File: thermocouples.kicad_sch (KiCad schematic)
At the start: 52 parts, among them J300 Conn_01x02_Pin, J301 Conn_01x02_Pin, J302 Conn_01x02_Pin, J303 Conn_01x02_Pin, U300 MAX31856, U301 MAX31856, U302 MAX31856, U303 MAX31856

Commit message: Some changes to power circuitry, more layout
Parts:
- C300, C301, C302, C303, C304, C305, C306, C307, C308, C309, C310, C311, C312, C313, C314, C315, C316, C317, C318, C319: footprint Capacitor_SMD:C_01005_0402Metric -> Capacitor_SMD:C_0402_1005Metric
- D300, D301, D302, D303: footprint Capacitor_SMD:C_01005_0402Metric -> LED_SMD:LED_0402_1005Metric
- R300, R301, R302, R303, R304, R305, R310, R311, R312, R313, R314, R315: footprint Resistor_SMD:R_0201_0603Metric -> Resistor_SMD:R_0603_1608Metric
- R306, R307, R308, R309, R316, R317, R318, R319: footprint Resistor_SMD:R_01005_0402Metric -> Resistor_SMD:R_0402_1005Metric
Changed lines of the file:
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@@
 			)
 		)
-		(property "Footprint" "Resistor_SMD:R_0201_0603Metric"
+		(property "Footprint" "Resistor_SMD:R_0603_1608Metric"
 			(at 174.244 84.074 90)
 			(effects
@@
 			)
 		)
-		(property "Footprint" "Resistor_SMD:R_01005_0402Metric"
+		(property "Footprint" "Resistor_SMD:R_0402_1005Metric"
 			(at 244.856 108.204 90)
 			(effects
@@
 			)
 		)
-		(property "Footprint" "Capacitor_SMD:C_01005_0402Metric"
+		(property "Footprint" "Capacitor_SMD:C_0402_1005Metric"
 			(at 69.5452 116.84 0)
 			(effects
@@
 			)
 		)
-		(property "Footprint" "Resistor_SMD:R_0201_0603Metric"
+		(property "Footprint" "Resistor_SMD:R_0603_1608Metric"
 			(at 35.814 61.214 90)
 			(effects
@@
 			)
 		)
-		(property "Footprint" "Capacitor_SMD:C_01005_0402Metric"
+		(property "Footprint" "Capacitor_SMD:C_0402_1005Metric"
 			(at 194.0052 48.26 0)
 			(effects
@@
 			)
 		)
-		(property "Footprint" "Capacitor_SMD:C_01005_0402Metric"
+		(property "Footprint" "Capacitor_SMD:C_0402_1005Metric"
 			(at 98.7552 48.26 0)
 			(effects
@@
 			)
 		)
-		(property "Footprint" "Resistor_SMD:R_0201_0603Metric"
+		(property "Footprint" "Resistor_SMD:R_0603_1608Metric"
 			(at 160.274 63.754 90)
 			(effects
@@
 			)
 		)
-		(property "Footprint" "Capacitor_SMD:C_01005_0402Metric"
+		(property "Footprint" "Capacitor_SMD:C_0402_1005Metric"
 			(at 51.7652 125.73 0)
 			(effects
@@
 			)
 		)
-		(property "Footprint" "Resistor_SMD:R_0201_0603Metric"
+		(property "Footprint" "Resistor_SMD:R_0603_1608Metric"
 			(at 160.274 61.214 90)
 			(effects
@@
 			)
 		)
-		(property "Footprint" "Resistor_SMD:R_0201_0603Metric"
+		(property "Footprint" "Resistor_SMD:R_0603_1608Metric"
 			(at 35.814 129.794 90)
 			(effects
@@
 			)
 		)
-		(property "Footprint" "Resistor_SMD:R_01005_0402Metric"
+		(property "Footprint" "Resistor_SMD:R_0402_1005Metric"
 			(at 120.396 39.624 90)
 			(effects
@@
 			)
 		)
-		(property "Footprint" "Capacitor_SMD:C_01005_0402Metric"
+		(property "Footprint" "Capacitor_SMD:C_0402_1005Metric"
 			(at 51.7652 135.89 0)
 			(effects
@@
 			)
 		)
-		(property "Footprint" "Resistor_SMD:R_0201_0603Metric"
+		(property "Footprint" "Resistor_SMD:R_0603_1608Metric"
 			(at 35.814 132.334 90)
 			(effects
@@
 			)
 		)
-		(property "Footprint" "Resistor_SMD:R_0201_0603Metric"
+		(property "Footprint" "Resistor_SMD:R_0603_1608Metric"
 			(at 160.274 132.334 90)
 			(effects
@@
 			)
 		)
-		(property "Footprint" "Capacitor_SMD:C_01005_0402Metric"
+		(property "Footprint" "Capacitor_SMD:C_0402_1005Metric"
 			(at 51.7652 57.15 0)
 			(effects
@@
 			)
 		)
-		(property "Footprint" "Capacitor_SMD:C_01005_0402Metric"
+		(property "Footprint" "Capacitor_SMD:C_0402_1005Metric"
 			(at 98.7552 116.84 0)
 			(effects
@@
 			)
 		)
-		(property "Footprint" "Capacitor_SMD:C_01005_0402Metric"
+		(property "Footprint" "Capacitor_SMD:C_0402_1005Metric"
 			(at 176.2252 135.89 0)
 			(effects
@@
 			)
 		)
-		(property "Footprint" "Capacitor_SMD:C_01005_0402Metric"
+		(property "Footprint" "Capacitor_SMD:C_0402_1005Metric"
 			(at 176.2252 125.73 0)
 			(effects
@@
 			)
 		)
-		(property "Footprint" "Resistor_SMD:R_01005_0402Metric"
+		(property "Footprint" "Resistor_SMD:R_0402_1005Metric"
 			(at 120.396 108.204 90)
 			(effects
@@
 			)
 		)
-		(property "Footprint" "Capacitor_SMD:C_01005_0402Metric"
+		(property "Footprint" "Capacitor_SMD:C_0402_1005Metric"
 			(at 176.2252 57.15 0)
 			(effects
@@
 			)
 		)
-		(property "Footprint" "Capacitor_SMD:C_01005_0402Metric"
+		(property "Footprint" "Capacitor_SMD:C_0402_1005Metric"
 			(at 51.7652 77.47 0)
 			(effects
@@
 			)
 		)
-		(property "Footprint" "Capacitor_SMD:C_01005_0402Metric"
+		(property "Footprint" "Capacitor_SMD:C_0402_1005Metric"
 			(at 176.2252 146.05 0)
 			(effects
@@
 			)
 		)
-		(property "Footprint" "Resistor_SMD:R_01005_0402Metric"
+		(property "Footprint" "Resistor_SMD:R_0402_1005Metric"
 			(at 234.696 49.784 90)
 			(effects
@@
 			)
 		)
-		(property "Footprint" "Resistor_SMD:R_0201_0603Metric"
+		(property "Footprint" "Resistor_SMD:R_0603_1608Metric"
 			(at 160.274 129.794 90)
 			(effects
@@
 			)
 		)
-		(property "Footprint" "Resistor_SMD:R_0201_0603Metric"
+		(property "Footprint" "Resistor_SMD:R_0603_1608Metric"
 			(at 49.784 152.654 90)
 			(effects
@@
 			)
 		)
-		(property "Footprint" "Capacitor_SMD:C_01005_0402Metric"
+		(property "Footprint" "LED_SMD:LED_0402_1005Metric"
 			(at 243.84 50.8 0)
 			(effects
@@
 			)
 		)
-		(property "Footprint" "Resistor_SMD:R_01005_0402Metric"
+		(property "Footprint" "Resistor_SMD:R_0402_1005Metric"
 			(at 234.696 118.364 90)
 			(effects
@@
 			)
 		)
-		(property "Footprint" "Capacitor_SMD:C_01005_0402Metric"
+		(property "Footprint" "Capacitor_SMD:C_0402_1005Metric"
 			(at 69.5452 48.26 0)
 			(effects
@@
 			)
 		)
-		(property "Footprint" "Capacitor_SMD:C_01005_0402Metric"
+		(property "Footprint" "Capacitor_SMD:C_0402_1005Metric"
 			(at 176.2252 77.47 0)
 			(effects
@@
 			)
 		)
-		(property "Footprint" "Resistor_SMD:R_01005_0402Metric"
+		(property "Footprint" "Resistor_SMD:R_0402_1005Metric"
 			(at 110.236 49.784 90)
 			(effects
@@
 			)
 		)
-		(property "Footprint" "Resistor_SMD:R_0201_0603Metric"
+		(property "Footprint" "Resistor_SMD:R_0603_1608Metric"
 			(at 35.814 63.754 90)
 			(effects
@@
 			)
 		)
-		(property "Footprint" "Capacitor_SMD:C_01005_0402Metric"
+		(property "Footprint" "Capacitor_SMD:C_0402_1005Metric"
 			(at 51.7652 67.31 0)
 			(effects
@@
 			)
 		)
-		(property "Footprint" "Resistor_SMD:R_01005_0402Metric"
+		(property "Footprint" "Resistor_SMD:R_0402_1005Metric"
 			(at 244.856 39.624 90)
 			(effects
@@
 			)
 		)
-		(property "Footprint" "Capacitor_SMD:C_01005_0402Metric"
+		(property "Footprint" "Capacitor_SMD:C_0402_1005Metric"
 			(at 194.0052 116.84 0)
 			(effects
@@
 			)
 		)
-		(property "Footprint" "Resistor_SMD:R_01005_0402Metric"
+		(property "Footprint" "Resistor_SMD:R_0402_1005Metric"
 			(at 110.236 118.364 90)
 			(effects
@@
 			)
 		)
-		(property "Footprint" "Capacitor_SMD:C_01005_0402Metric"
+		(property "Footprint" "LED_SMD:LED_0402_1005Metric"
 			(at 119.38 50.8 0)
 			(effects
@@
 			)
 		)
-		(property "Footprint" "Capacitor_SMD:C_01005_0402Metric"
+		(property "Footprint" "Capacitor_SMD:C_0402_1005Metric"
 			(at 223.2152 48.26 0)
 			(effects
@@
 			)
 		)
-		(property "Footprint" "Capacitor_SMD:C_01005_0402Metric"
+		(property "Footprint" "Capacitor_SMD:C_0402_1005Metric"
 			(at 51.7652 146.05 0)
 			(effects
@@
 			)
 		)
-		(property "Footprint" "Capacitor_SMD:C_01005_0402Metric"
+		(property "Footprint" "Capacitor_SMD:C_0402_1005Metric"
 			(at 176.2252 67.31 0)
 			(effects
@@
 			)
 		)
-		(property "Footprint" "Capacitor_SMD:C_01005_0402Metric"
+		(property "Footprint" "Capacitor_SMD:C_0402_1005Metric"
 			(at 223.2152 116.84 0)
 			(effects
@@
 			)
 		)
-		(property "Footprint" "Resistor_SMD:R_0201_0603Metric"
+		(property "Footprint" "Resistor_SMD:R_0603_1608Metric"
 			(at 49.784 84.074 90)
 			(effects
@@
 			)
 		)
-		(property "Footprint" "Resistor_SMD:R_0201_0603Metric"
+		(property "Footprint" "Resistor_SMD:R_0603_1608Metric"
 			(at 174.244 152.654 90)
 			(effects
@@
 			)
 		)
-		(property "Footprint" "Capacitor_SMD:C_01005_0402Metric"
+		(property "Footprint" "LED_SMD:LED_0402_1005Metric"
 			(at 243.84 119.38 0)
 			(effects
@@
 			)
 		)
-		(property "Footprint" "Capacitor_SMD:C_01005_0402Metric"
+		(property "Footprint" "LED_SMD:LED_0402_1005Metric"
 			(at 119.38 119.38 0)
 			(effects

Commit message: Extremely incomplete, preliminary, pre-alpha, ugly layout
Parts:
- renumbered C306 to C300, C308 to C301, C316 to C302, C318 to C303, C300 to C304, C310 to C305, C301 to C306, C311 to C307, C302 to C308, C312 to C309, C307 to C310, C309 to C311, C317 to C312, C319 to C313, C303 to C314, C313 to C315, C304 to C316, C314 to C317, C305 to C318, C315 to C319, D302 to D301, D301 to D302, J302 to J301, J301 to J302, R308 to R300, R318 to R301, R306 to R302, R316 to R303, R300 to R304, R310 to R305, R301 to R306, R311 to R307, R304 to R308, R314 to R309, R309 to R310, R319 to R311, R307 to R312, R317 to R313, R302 to R314, R312 to R315, R303 to R316, R313 to R317, R305 to R318, R315 to R319, U302 to U301, U301 to U302
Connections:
- net +3.3V is gone; now on net +3V3: R302.1, R303.1, R312.1, R313.1

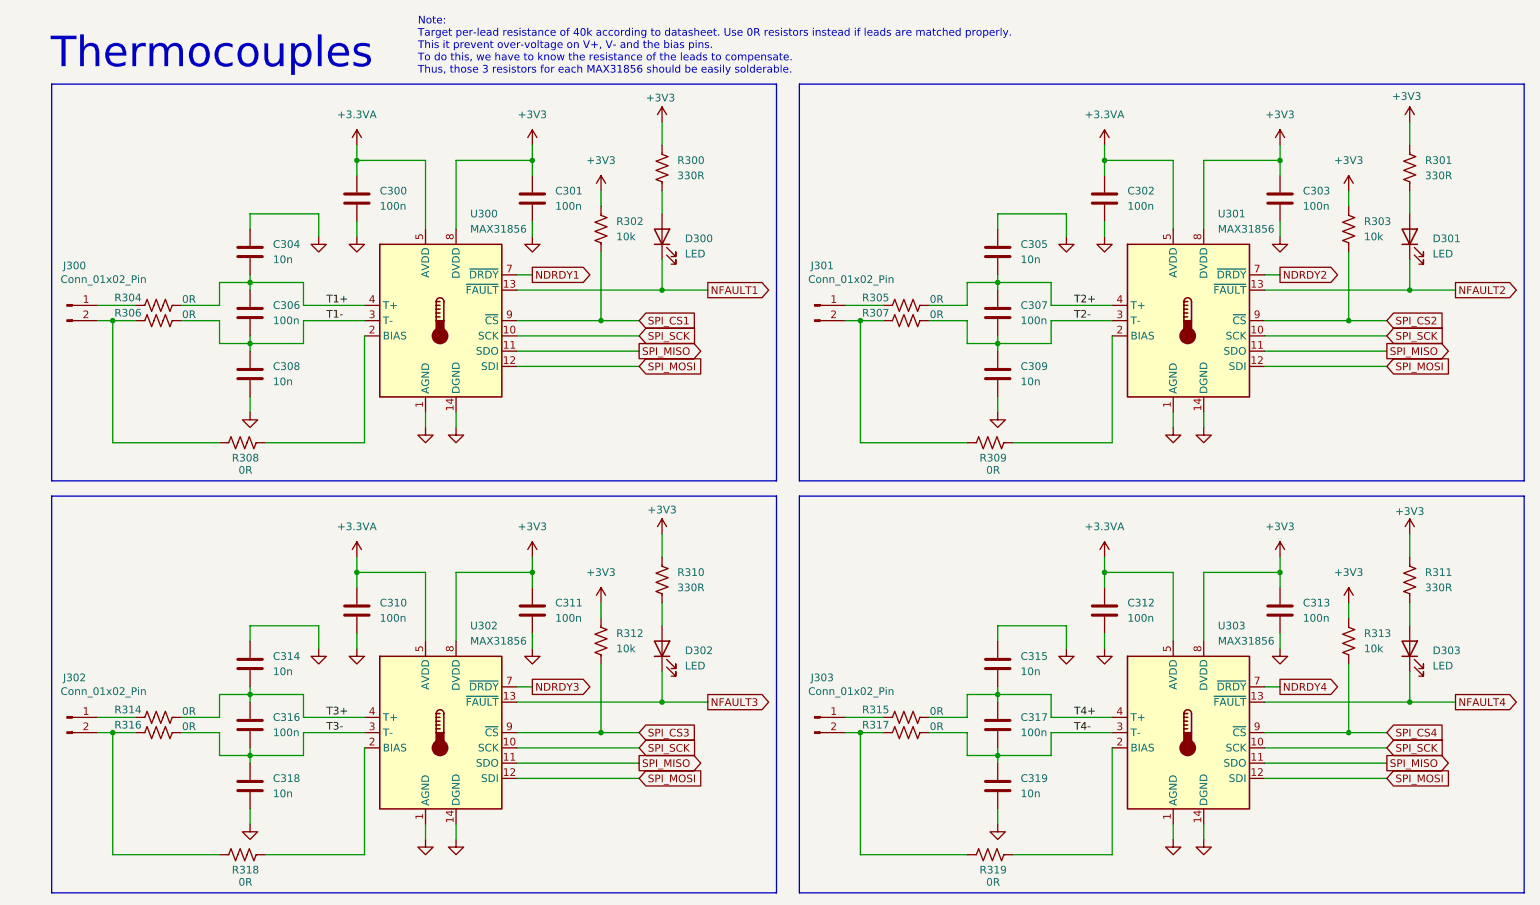
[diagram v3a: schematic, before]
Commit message: First decent layout
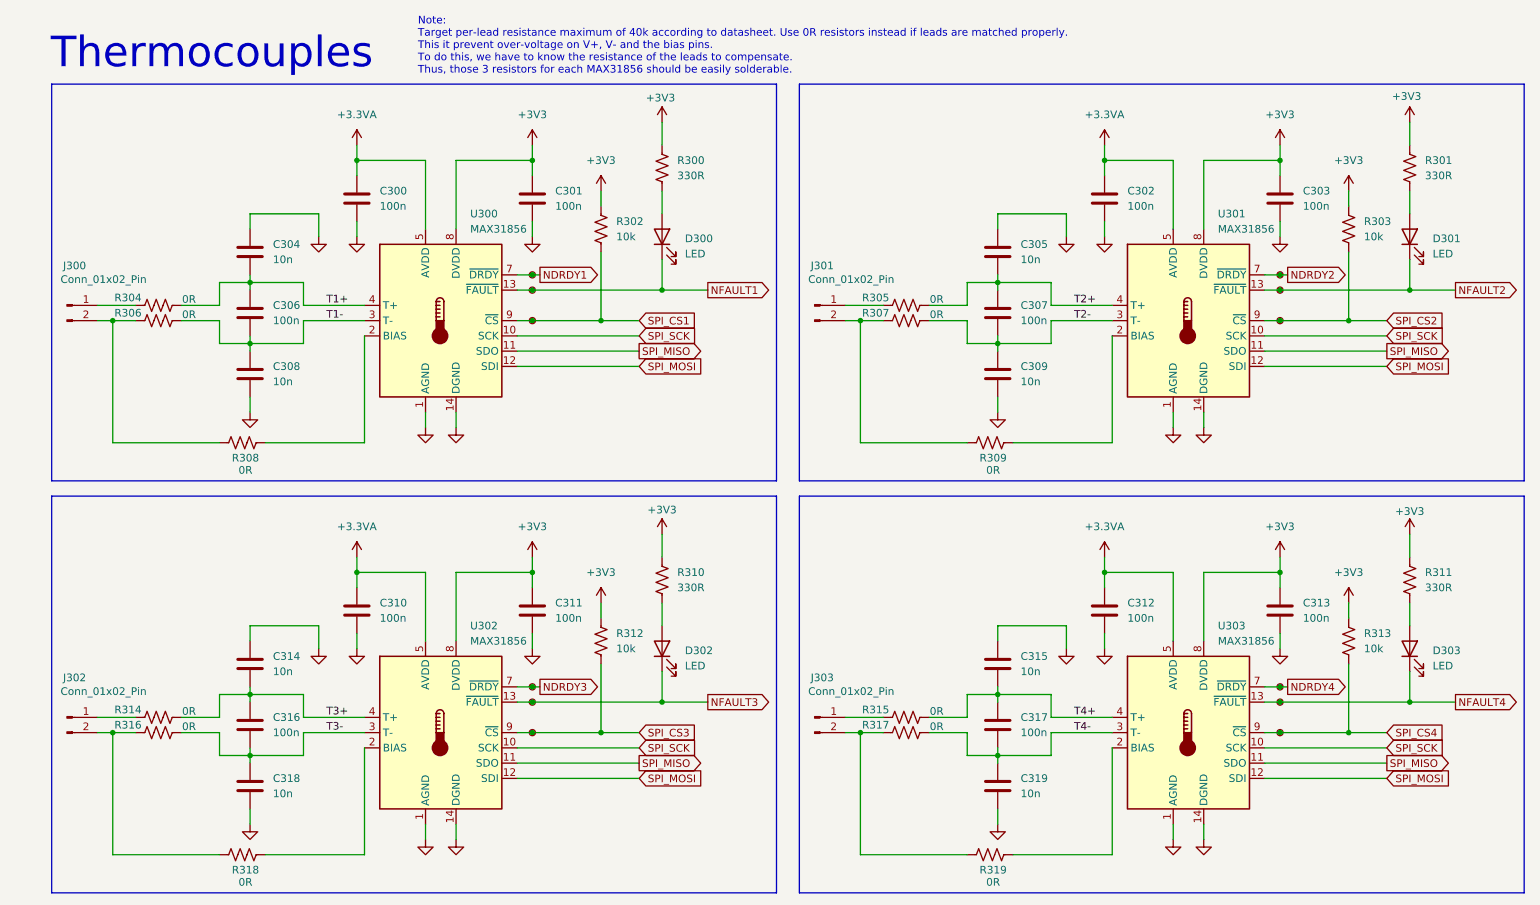
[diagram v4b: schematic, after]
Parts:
- added TP106, TP107, TP108, TP109, TP110, TP114, TP115, TP116, TP120, TP121, TP122, TP300: TestPoint_Small, TestPoint:TestPoint_Pad_D1.0mm, symbol Connector:TestPoint_Small
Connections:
- net NDRDY1: now also TP106.1
- net NDRDY2: now also TP114.1
- net NDRDY3: now also TP108.1
- net NDRDY4: now also TP120.1
- net NFAULT1: now also TP107.1
- net NFAULT2: now also TP115.1
- net NFAULT3: now also TP109.1
- net NFAULT4: now also TP121.1
- net SPI_CS1: now also TP300.1
- net SPI_CS2: now also TP116.1
- net SPI_CS3: now also TP110.1
- net SPI_CS4: now also TP122.1
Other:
- note added: "Note: Target per-lead resistance maximum of 40k according to datasheet. Use 0R resistors instead if leads are matched properly. This it prevent over-voltage on V+, V- and the bias pins. To do this, we have to know the resistance of the leads to compensate. Thus, those 3 resistors for each MAX31856 should be easily solderable."
- note removed: "Note: Target per-lead resistance of 40k according to datasheet. Use 0R resistors instead if leads are matched properly. This it prevent over-voltage on V+, V- and the bias pins. To do this, we have to know the resistance of the leads to compensate. Thus, those 3 resistors for each MAX31856 should be easily solderable."

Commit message: I hate everything
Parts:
- removed J300, J301, J302, J303: Conn_01x02_Pin, Connector_PinHeader_2.54mm:PinHeader_1x02_P2.54mm_Vertical, symbol Connector:Conn_01x02_Pin
- added J105, J106, J107, J108: PCC-SMP-K-5, PCCSMPK5, symbol PCC-SMP-K-5:PCC-SMP-K-5
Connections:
- net GND: now also J105.MH1, J105.MH2, J106.MH1, J106.MH2, J107.MH1, J107.MH2, J108.MH1, J108.MH2
- net T2_IN-: now reaches R307.1, R309.1
- net T2_IN-: now also J106.1 (K)
- net T1_IN+: now reaches R304.1
- net T1_IN+: now also J105.2 (+), J107.2 (+)
- net T2_IN+: now reaches R305.1
- net T2_IN+: now also J106.2 (+)
- net T3_IN+: now reaches R314.1
- net T3_IN-: now reaches R316.1, R318.1
- net T4_IN-: now reaches R317.1, R319.1
- net T4_IN-: now also J108.1 (K)
- net T1_IN-: now reaches R306.1, R308.1
- net T1_IN-: now also J105.1 (K), J107.1 (K)
- net T4_IN+: now reaches R315.1
- net T4_IN+: now also J108.2 (+)

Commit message: First workable layout
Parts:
- C300, C301, C302, C303, C306, C307, C310, C311, C312, C313, C316, C317: LCSC (none) -> C1525
- C304, C305, C308, C309, C314, C315, C318, C319: LCSC (none) -> C15195
- D300, D301, D302, D303: LCSC (none) -> C965793
- R300, R301, R310, R311: LCSC (none) -> C105875
- R302, R303, R312, R313: LCSC (none) -> C60490
- R304, R305, R306, R307, R308, R309, R314, R315, R316, R317, R318, R319: LCSC (none) -> C95177
- U300, U301, U302, U303: LCSC (none) -> C2653162
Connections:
- net T1_IN+: no longer J107.2 (+)
- net T1_IN-: no longer J107.1 (K)
- net T3_IN+: now also J107.2 (+)
- net T3_IN-: now also J107.1 (K)

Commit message: Added pfet for reverse polarity protection, moved power circuitry away from analog parts
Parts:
- J105, J106, J107, J108: footprint PCCSMPK5 -> Omega:PCCSMPK5
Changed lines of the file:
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@@
 			)
 		)
-		(property "Footprint" "PCCSMPK5"
+		(property "Footprint" "Omega:PCCSMPK5"
 			(at 172.72 131.75 0)
 			(effects
@@
 			)
 		)
-		(property "Footprint" "PCCSMPK5"
+		(property "Footprint" "Omega:PCCSMPK5"
 			(at 175.26 199.06 0)
 			(effects
@@
 			)
 		)
-		(property "Footprint" "PCCSMPK5"
+		(property "Footprint" "Omega:PCCSMPK5"
 			(at 49.53 200.33 0)
 			(effects
@@
 			)
 		)
-		(property "Footprint" "PCCSMPK5"
+		(property "Footprint" "Omega:PCCSMPK5"
 			(at 49.53 130.48 0)
 			(effects

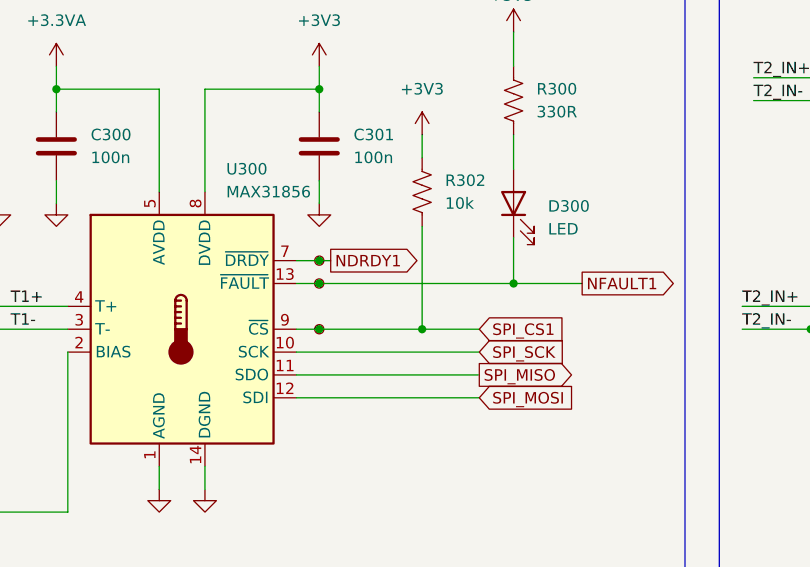
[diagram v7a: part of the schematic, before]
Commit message: Modify repo for usage on Linux, add basic CI
chore: fix CI

Small things
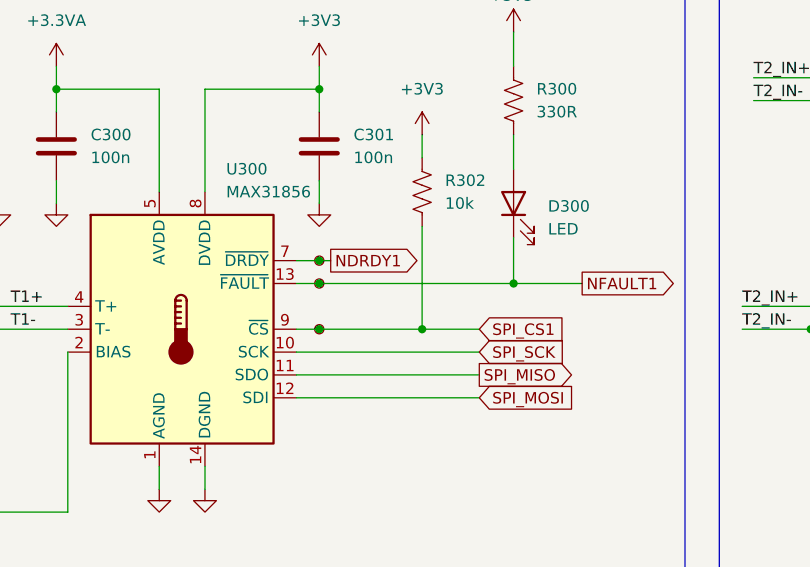
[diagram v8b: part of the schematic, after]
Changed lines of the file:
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@@
 	)
 	(junction
-		(at 97.7804 59.69)
+		(at 97.79 59.69)
 		(diameter 0)
 		(color 0 0 0 0)
@@
 	(wire
 		(pts
-			(xy 95.25 59.69) (xy 97.7804 59.69)
+			(xy 95.25 59.69) (xy 97.79 59.69)
 		)
 		(stroke
@@
 	(wire
 		(pts
-			(xy 97.7804 59.69) (xy 119.38 59.69)
+			(xy 97.79 59.69) (xy 119.38 59.69)
 		)
 		(stroke
@@
 	(symbol
 		(lib_id "Connector:TestPoint_Small")
-		(at 97.7804 59.69 0)
+		(at 97.79 59.69 0)
 		(unit 1)
 		(exclude_from_sim no)
@@
 		(dnp no)
 		(property "Reference" "TP107"
-			(at 98.7964 58.674 0)
+			(at 98.806 58.674 0)
 			(effects
 				(font
@@
 		)
 		(property "Value" "TestPoint_Small"
-			(at 99.0504 60.9599 0)
+			(at 99.06 60.9599 0)
 			(effects
 				(font
@@
 		)
 		(property "Footprint" "TestPoint:TestPoint_Pad_D1.0mm"
-			(at 102.8604 59.69 0)
+			(at 102.87 59.69 0)
 			(effects
 				(font
@@
 		)
 		(property "Datasheet" "~"
-			(at 102.8604 59.69 0)
+			(at 102.87 59.69 0)
 			(effects
 				(font
@@
 		)
 		(property "Description" "test point"
-			(at 97.7804 59.69 0)
+			(at 97.79 59.69 0)
 			(effects
 				(font
